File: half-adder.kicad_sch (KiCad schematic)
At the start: 0 parts

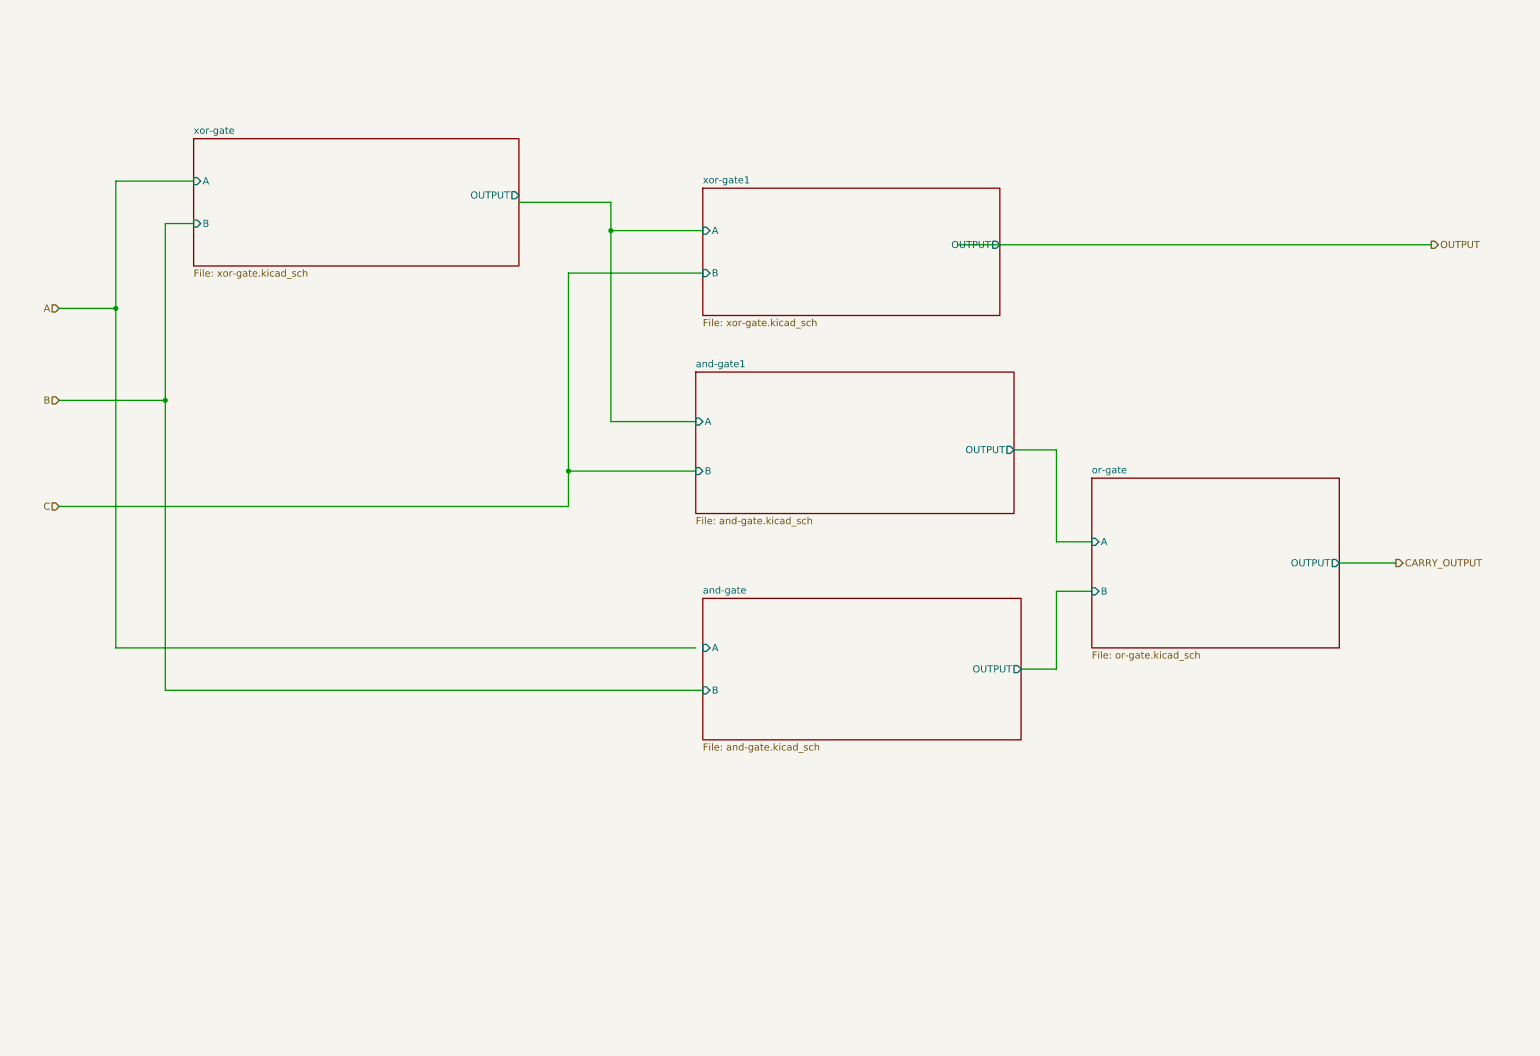
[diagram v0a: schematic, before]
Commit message: Create PCB layout
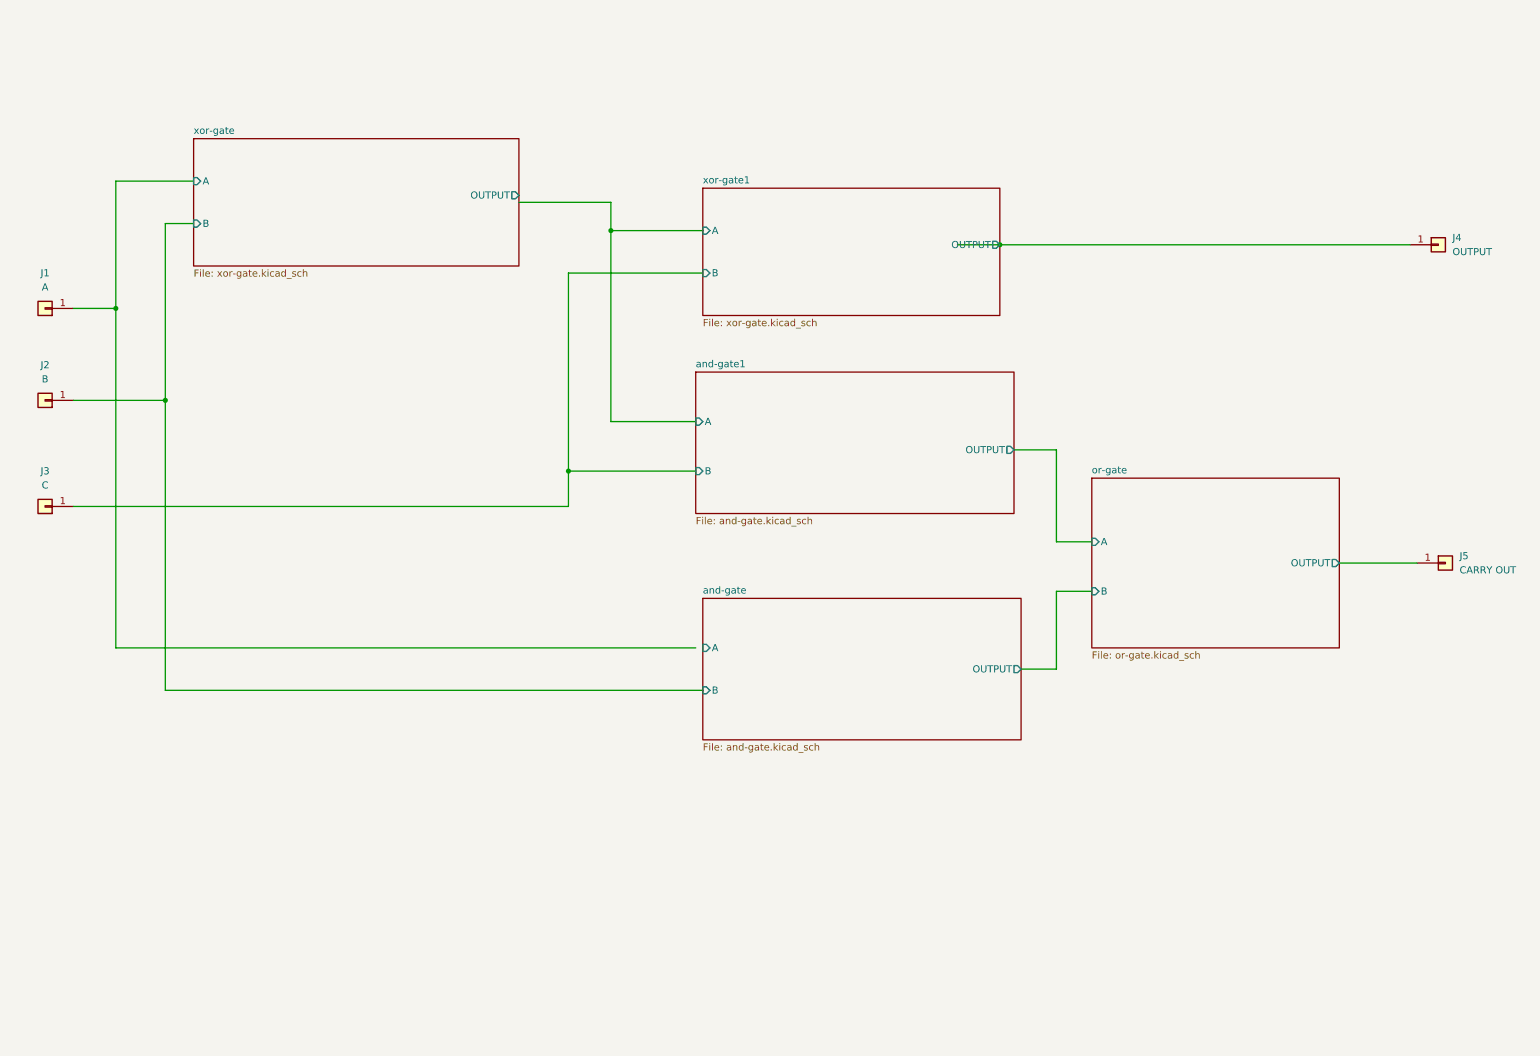
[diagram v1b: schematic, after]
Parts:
- added J1: A, Connector_PinHeader_2.54mm:PinHeader_1x01_P2.54mm_Vertical, symbol Connector_Generic:Conn_01x01
- added J2: B, Connector_PinHeader_2.54mm:PinHeader_1x01_P2.54mm_Vertical, symbol Connector_Generic:Conn_01x01
- added J3: C, Connector_PinHeader_2.54mm:PinHeader_1x01_P2.54mm_Vertical, symbol Connector_Generic:Conn_01x01
- added J4: OUTPUT, Connector_PinHeader_2.54mm:PinHeader_1x01_P2.54mm_Vertical, symbol Connector_Generic:Conn_01x01
- added J5: CARRY OUT, Connector_PinHeader_2.54mm:PinHeader_1x01_P2.54mm_Vertical, symbol Connector_Generic:Conn_01x01
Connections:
- net xor-gate1/OUTPUT: now also J4.1 (Pin_1)
- new net and-gate/B: J2.1 (Pin_1)
- new net and-gate1/B: J3.1 (Pin_1)
- new net or-gate/OUTPUT: J5.1 (Pin_1)
- new net xor-gate/A: J1.1 (Pin_1)
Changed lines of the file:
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@@
 (kicad_sch (version 20230121) (generator eeschema)
   (paper "A4")
+  (junction (at 190.5 54.61) (diameter 0) (color 0 0 0 0)
+  )
   (junction (at 40.64 82.55) (diameter 0) (color 0 0 0 0)
   )
@@
     (stroke (width 0) (type default))
   )
-  (wire (pts (xy 21.59 82.55) (xy 40.64 82.55))
-    (stroke (width 0) (type default))
-  )
-  (wire (pts (xy 182.88 54.61) (xy 267.97 54.61))
+  (wire (pts (xy 24.13 82.55) (xy 40.64 82.55))
+    (stroke (width 0) (type default))
+  )
+  (wire (pts (xy 182.88 54.61) (xy 190.5 54.61))
     (stroke (width 0) (type default))
   )
@@
     (stroke (width 0) (type default))
   )
-  (wire (pts (xy 251.46 111.76) (xy 261.62 111.76))
+  (wire (pts (xy 251.46 111.76) (xy 265.43 111.76))
     (stroke (width 0) (type default))
   )
@@
     (stroke (width 0) (type default))
   )
-  (wire (pts (xy 21.59 101.6) (xy 113.03 101.6))
+  (wire (pts (xy 24.13 101.6) (xy 113.03 101.6))
     (stroke (width 0) (type default))
   )
@@
     (stroke (width 0) (type default))
   )
-  (wire (pts (xy 21.59 66.04) (xy 31.75 66.04))
+  (wire (pts (xy 190.5 54.61) (xy 264.16 54.61))
+    (stroke (width 0) (type default))
+  )
+  (wire (pts (xy 24.13 66.04) (xy 31.75 66.04))
     (stroke (width 0) (type default))
   )
@@
     (stroke (width 0) (type default))
   )
-  (hierarchical_label "CARRY_OUTPUT" (shape output) (at 261.62 111.76 0) (fields_autoplaced)
-    (effects (font (size 1.27 1.27)) (justify left))
-  )
-  (hierarchical_label "A" (shape input) (at 21.59 66.04 180) (fields_autoplaced)
-    (effects (font (size 1.27 1.27)) (justify right))
-  )
-  (hierarchical_label "B" (shape input) (at 21.59 82.55 180) (fields_autoplaced)
-    (effects (font (size 1.27 1.27)) (justify right))
-  )
-  (hierarchical_label "C" (shape input) (at 21.59 101.6 180) (fields_autoplaced)
-    (effects (font (size 1.27 1.27)) (justify right))
-  )
-  (hierarchical_label "OUTPUT" (shape output) (at 267.97 54.61 0) (fields_autoplaced)
-    (effects (font (size 1.27 1.27)) (justify left))
+  (symbol (lib_id "Connector_Generic:Conn_01x01") (at 270.51 111.76 0) (unit 1)
+    (in_bom yes) (on_board yes) (dnp no) (fields_autoplaced)
+    (property "Reference" "J5" (at 273.05 110.49 0)
+      (effects (font (size 1.27 1.27)) (justify left))
+    )
+    (property "Value" "CARRY OUT" (at 273.05 113.03 0)
+      (effects (font (size 1.27 1.27)) (justify left))
+    )
+    (property "Footprint" "Connector_PinHeader_2.54mm:PinHeader_1x01_P2.54mm_Vertical" (at 270.51 111.76 0)
+      (effects (font (size 1.27 1.27)) hide)
+    )
+    (property "Datasheet" "~" (at 270.51 111.76 0)
+      (effects (font (size 1.27 1.27)) hide)
+    )
+    (pin "1")
+    (instances
+      (project "half-adder"
+        (path "/88c27409-0a88-4cf1-8b65-cf7271709e32"
+          (reference "J5") (unit 1)
+        )
+      )
+    )
+  )
+  (symbol (lib_id "Connector_Generic:Conn_01x01") (at 269.24 54.61 0) (unit 1)
+    (in_bom yes) (on_board yes) (dnp no) (fields_autoplaced)
+    (property "Reference" "J4" (at 271.78 53.34 0)
+      (effects (font (size 1.27 1.27)) (justify left))
+    )
+    (property "Value" "OUTPUT" (at 271.78 55.88 0)
+      (effects (font (size 1.27 1.27)) (justify left))
+    )
+    (property "Footprint" "Connector_PinHeader_2.54mm:PinHeader_1x01_P2.54mm_Vertical" (at 269.24 54.61 0)
+      (effects (font (size 1.27 1.27)) hide)
+    )
+    (property "Datasheet" "~" (at 269.24 54.61 0)
+      (effects (font (size 1.27 1.27)) hide)
+    )
+    (pin "1")
+    (instances
+      (project "half-adder"
+        (path "/88c27409-0a88-4cf1-8b65-cf7271709e32"
+          (reference "J4") (unit 1)
+        )
+      )
+    )
+  )
+  (symbol (lib_id "Connector_Generic:Conn_01x01") (at 19.05 66.04 180) (unit 1)
+    (in_bom yes) (on_board yes) (dnp no) (fields_autoplaced)
+    (property "Reference" "J1" (at 19.05 59.69 0)
+      (effects (font (size 1.27 1.27)))
+    )
+    (property "Value" "A" (at 19.05 62.23 0)
+      (effects (font (size 1.27 1.27)))
+    )
+    (property "Footprint" "Connector_PinHeader_2.54mm:PinHeader_1x01_P2.54mm_Vertical" (at 19.05 66.04 0)
+      (effects (font (size 1.27 1.27)) hide)
+    )
+    (property "Datasheet" "~" (at 19.05 66.04 0)
+      (effects (font (size 1.27 1.27)) hide)
+    )
+    (pin "1")
+    (instances
+      (project "half-adder"
+        (path "/88c27409-0a88-4cf1-8b65-cf7271709e32"
+          (reference "J1") (unit 1)
+        )
+      )
+    )
+  )
+  (symbol (lib_id "Connector_Generic:Conn_01x01") (at 19.05 82.55 180) (unit 1)
+    (in_bom yes) (on_board yes) (dnp no) (fields_autoplaced)
+    (property "Reference" "J2" (at 19.05 76.2 0)
+      (effects (font (size 1.27 1.27)))
+    )
+    (property "Value" "B" (at 19.05 78.74 0)
+      (effects (font (size 1.27 1.27)))
+    )
+    (property "Footprint" "Connector_PinHeader_2.54mm:PinHeader_1x01_P2.54mm_Vertical" (at 19.05 82.55 0)
+      (effects (font (size 1.27 1.27)) hide)
+    )
+    (property "Datasheet" "~" (at 19.05 82.55 0)
+      (effects (font (size 1.27 1.27)) hide)
+    )
+    (pin "1")
+    (instances
+      (project "half-adder"
+        (path "/88c27409-0a88-4cf1-8b65-cf7271709e32"
+          (reference "J2") (unit 1)
+        )
+      )
+    )
+  )
+  (symbol (lib_id "Connector_Generic:Conn_01x01") (at 19.05 101.6 180) (unit 1)
+    (in_bom yes) (on_board yes) (dnp no) (fields_autoplaced)
+    (property "Reference" "J3" (at 19.05 95.25 0)
+      (effects (font (size 1.27 1.27)))
+    )
+    (property "Value" "C" (at 19.05 97.79 0)
+      (effects (font (size 1.27 1.27)))
+    )
+    (property "Footprint" "Connector_PinHeader_2.54mm:PinHeader_1x01_P2.54mm_Vertical" (at 19.05 101.6 0)
+      (effects (font (size 1.27 1.27)) hide)
+    )
+    (property "Datasheet" "~" (at 19.05 101.6 0)
+      (effects (font (size 1.27 1.27)) hide)
+    )
+    (pin "1")
+    (instances
+      (project "half-adder"
+        (path "/88c27409-0a88-4cf1-8b65-cf7271709e32"
+          (reference "J3") (unit 1)
+        )
+      )
+    )
   )
   (sheet (at 207.01 96.52) (size 44.45 30.48) (fields_autoplaced)

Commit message: Create schematic without hierarchical schematics
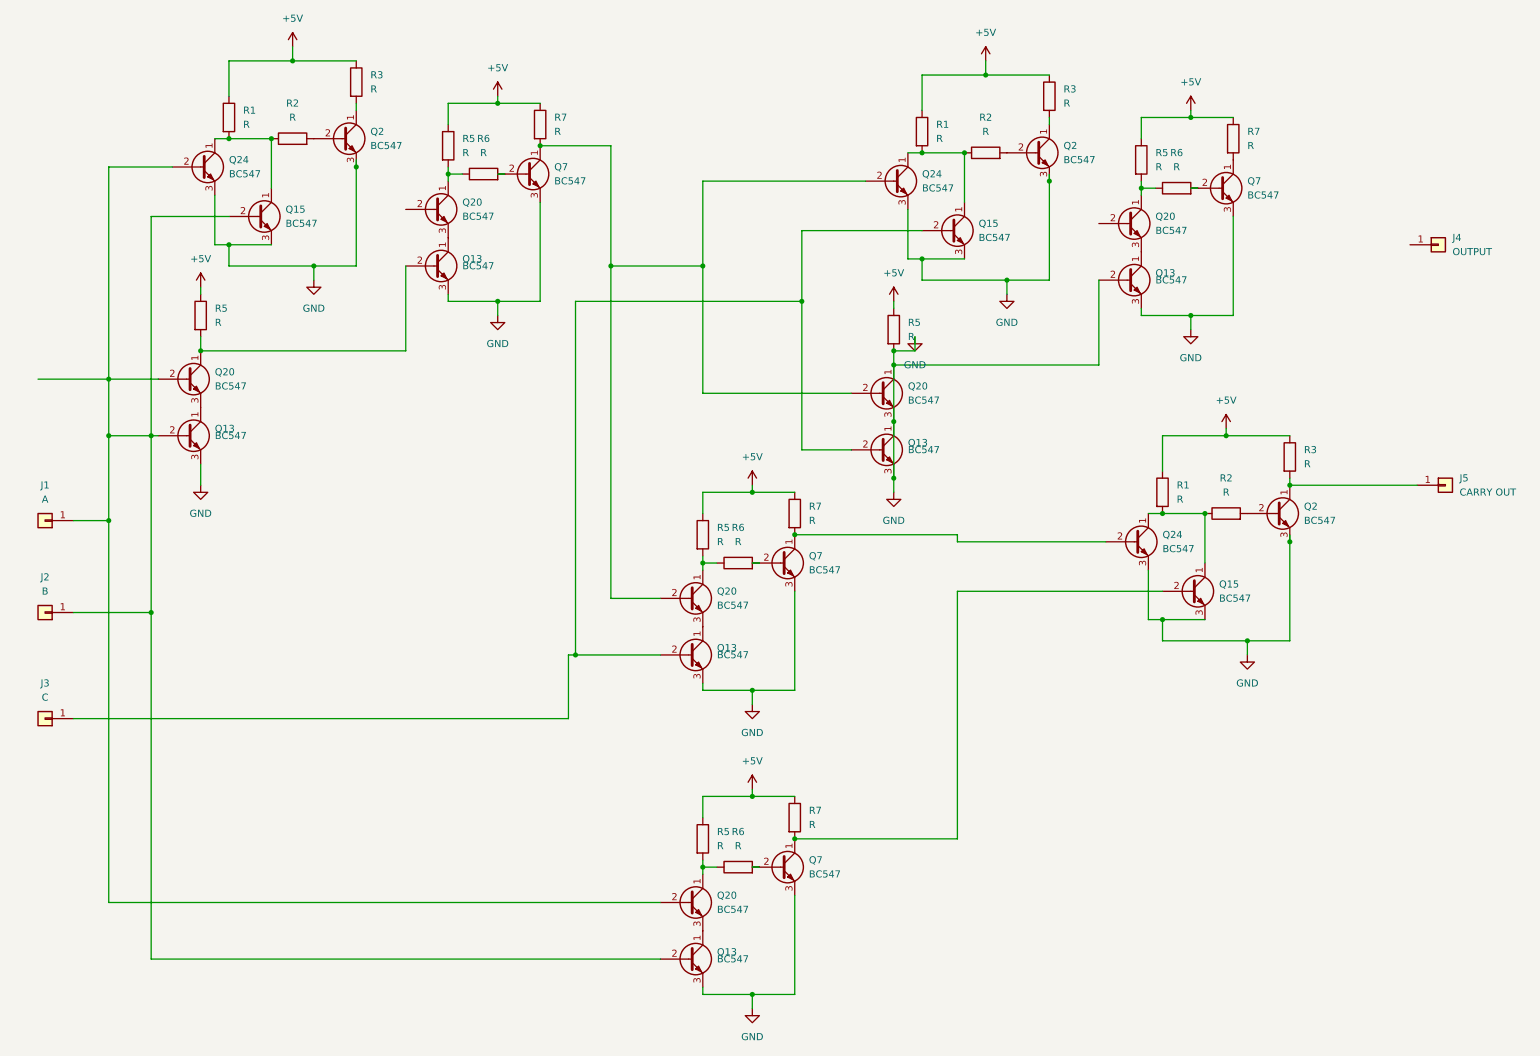
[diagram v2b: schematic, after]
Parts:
- added Q13 (x6), Q15 (x3), Q2 (x3), Q20 (x6), Q24 (x3), Q7 (x4): BC547, Package_TO_SOT_THT:TO-92_Inline, symbol Transistor_BJT:BC547
- added R1 (x3), R2 (x3), R3 (x3), R5 (x6), R6 (x4), R7 (x4): R, Resistor_SMD:R_0201_0603Metric, symbol Device:R
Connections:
- net xor-gate/A is gone; now on an unnamed net: J1.1 (Pin_1)
- net and-gate/B: no longer names the net of J2.1 (Pin_1)
- net and-gate/B: now also Q13.2 (B), Q13.2 (B), Q15.2 (B), Q20.2 (B), Q20.2 (B), Q24.2 (B)
- net and-gate1/B: no longer names the net of J3.1 (Pin_1)
- net and-gate1/B: now also Q13.2 (B), Q13.2 (B), Q15.2 (B)
- net or-gate/OUTPUT: no longer names the net of J5.1 (Pin_1)
- net or-gate/OUTPUT: now also Q2.1 (C), R3.2
- net xor-gate1/OUTPUT: no longer names the net of J4.1 (Pin_1)
- new net: Q15.1 (C), Q24.1 (C), R1.2, R2.1 (x3)
- new net: Q2.1 (C), R3.2 (x2)
- new net: Q2.2 (B), R2.2 (x3)
- new net: Q20.1 (C), R5.2, R6.1 (x4)
- new net: Q7.1 (C), R7.2
- new net: Q7.2 (B), R6.2 (x4)
- new net: Q20.2 (B), Q20.2 (B), Q24.2 (B), Q7.1 (C), R7.2
- new net: Q13.1 (C), Q20.3 (E) (x5)
- new net: Q15.2 (B), Q7.1 (C), R7.2
- new net: Q13.2 (B), Q20.1 (C), R5.2
- new net: Q24.2 (B), Q7.1 (C), R7.2
- new net +5V: R1.1, R1.1, R1.1, R3.1, R3.1, R3.1, R5.1, R5.1, R5.1, R5.1, R5.1, R5.1, R7.1, R7.1, R7.1, R7.1
- new net GND: Q13.1 (C), Q13.2 (B), Q13.3 (E), Q13.3 (E), Q13.3 (E), Q13.3 (E), Q13.3 (E), Q13.3 (E), Q15.3 (E), Q15.3 (E), Q15.3 (E), Q2.3 (E), Q2.3 (E), Q2.3 (E), Q20.1 (C), Q20.3 (E), Q24.3 (E), Q24.3 (E), Q24.3 (E), Q7.3 (E), Q7.3 (E), Q7.3 (E), Q7.3 (E), R5.2
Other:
- removed sheet and-gate
- removed sheet and-gate1
- removed sheet or-gate
- removed sheet xor-gate
- removed sheet xor-gate1
- moved on the sheet: J1, J2, J3, J5
